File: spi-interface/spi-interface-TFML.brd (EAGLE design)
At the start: 50.8 x 63.5 mm, 112 parts, among them Q1 AO3402, Q2 AO3402, U1 LY3200, U10 NC7SZ, U11 SI822X, U2 LY3200, U3 LY3200, U4 ADXL335, U7 MAX9174, U8 MAX9174, U9 MAX9174

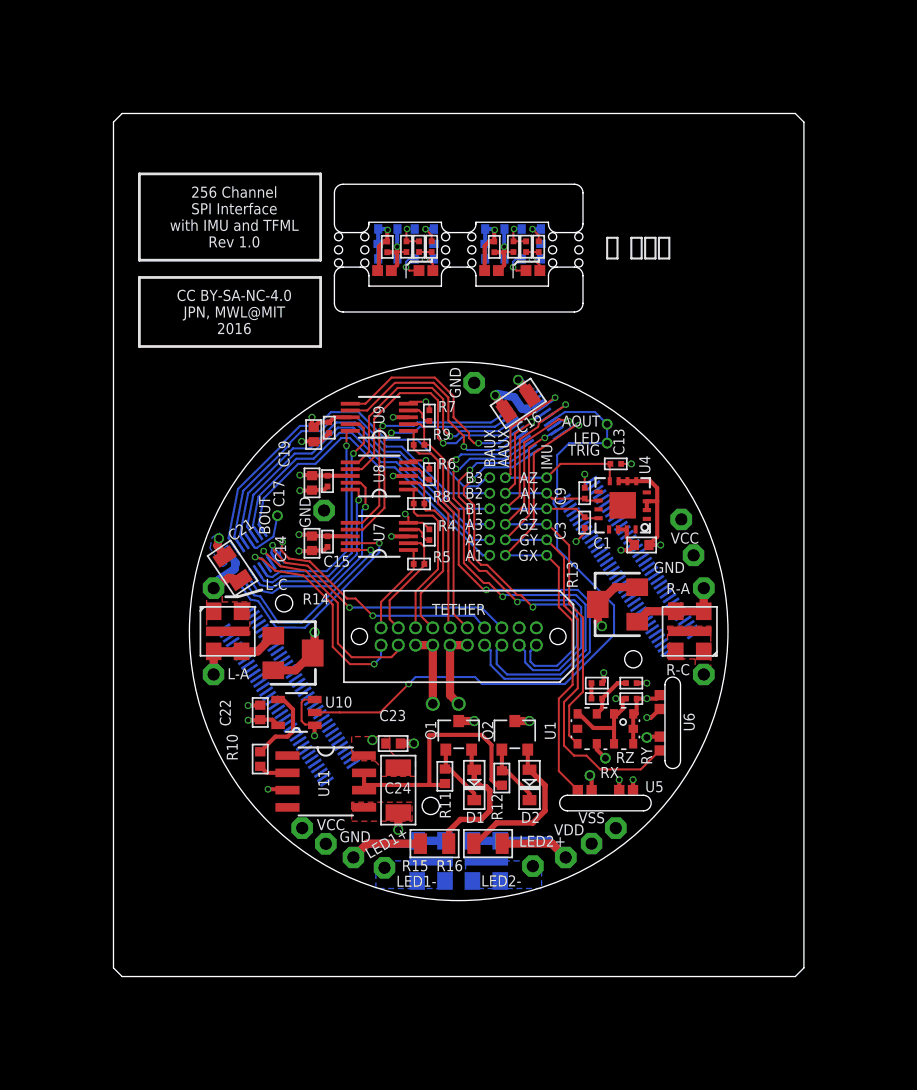
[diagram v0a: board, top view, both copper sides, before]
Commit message: Modified SPI interface board outline
- The SPI interface board itself was not properly tab routed
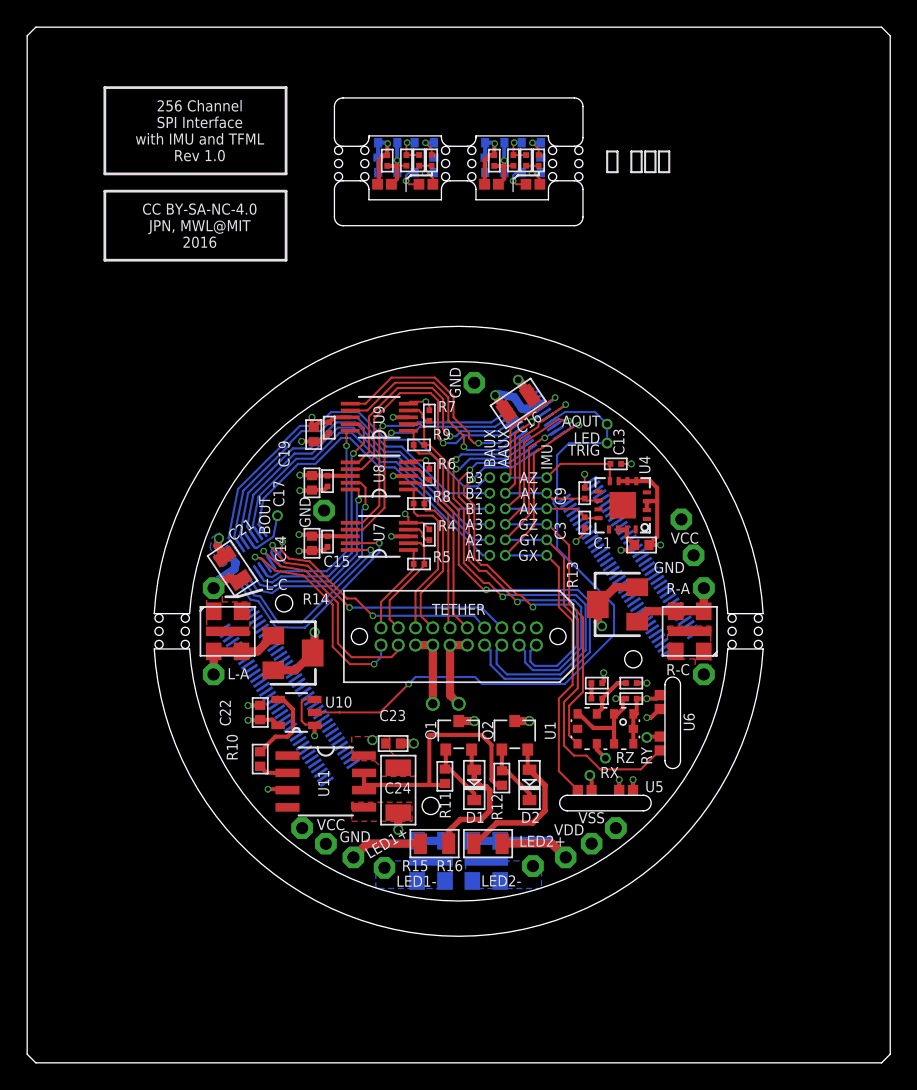
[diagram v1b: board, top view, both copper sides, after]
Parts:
- moved C11 6.35 mm to (-2.92, 34.7)
- moved C4 6.35 mm to (-5.26, 34.6)
- moved C5 6.35 mm to (2.62, 34.6)
- moved C7 6.35 mm to (-3.85, 34.7)
- moved C8 6.35 mm to (4.03, 34.7)
- moved R2 6.35 mm to (-1.99, 34.7)
- moved R3 6.35 mm to (5.88, 34.7)
- moved C12 6.35 mm to (4.96, 34.7)
- moved TP1 6.35 mm to (-5.97, 32.9)
- moved TP2 6.35 mm to (-1.90, 32.9)
- moved TP3 6.35 mm to (1.90, 32.9)
- moved TP4 6.35 mm to (5.97, 32.9)
- moved TP5 6.35 mm to (-2.92, 32.9)
- moved TP6 6.35 mm to (4.95, 32.9)
- moved TP7 6.35 mm to (-4.95, 32.9)
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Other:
- board size 50.8 x 63.5 mm -> 63.5 x 76.2 mm
